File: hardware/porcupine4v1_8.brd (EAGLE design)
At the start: 24.4 x 27.4 mm, 33 parts, among them X1 PROGCON

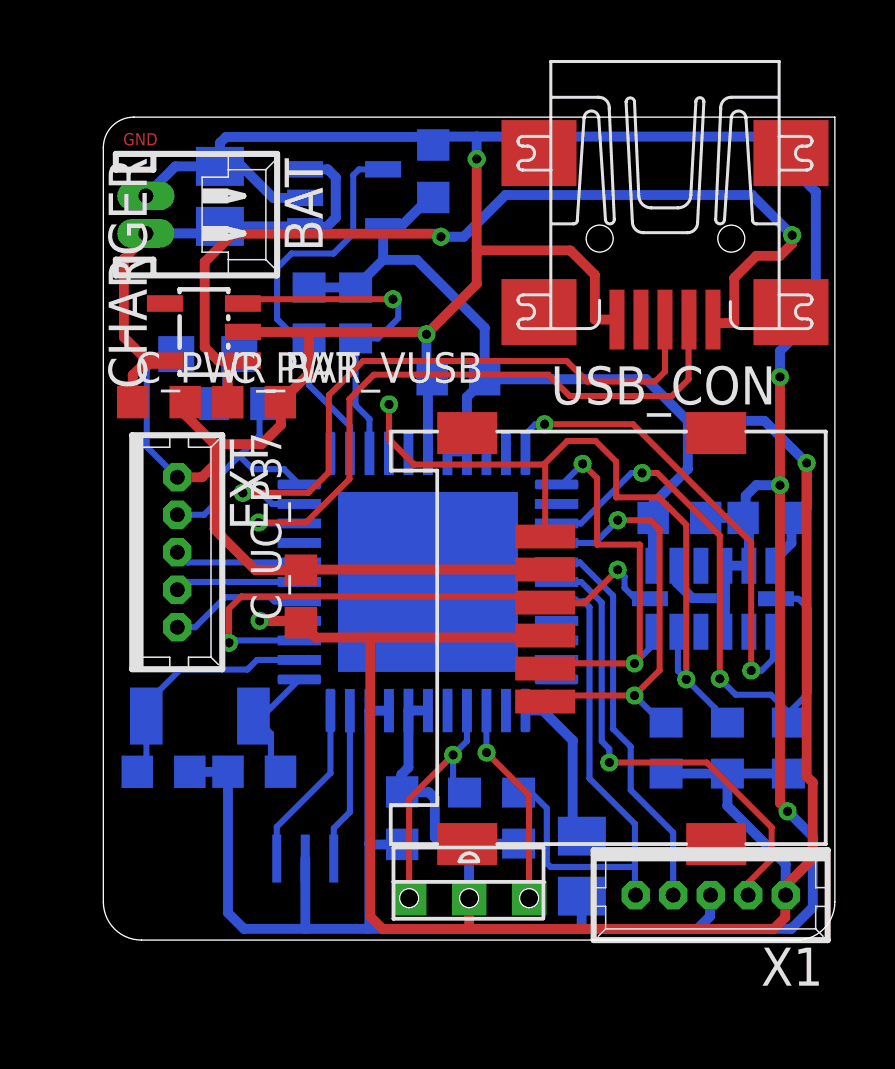
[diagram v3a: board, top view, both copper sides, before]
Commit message: porcupine4v1_8: updated extension pins (names), shifted some vias
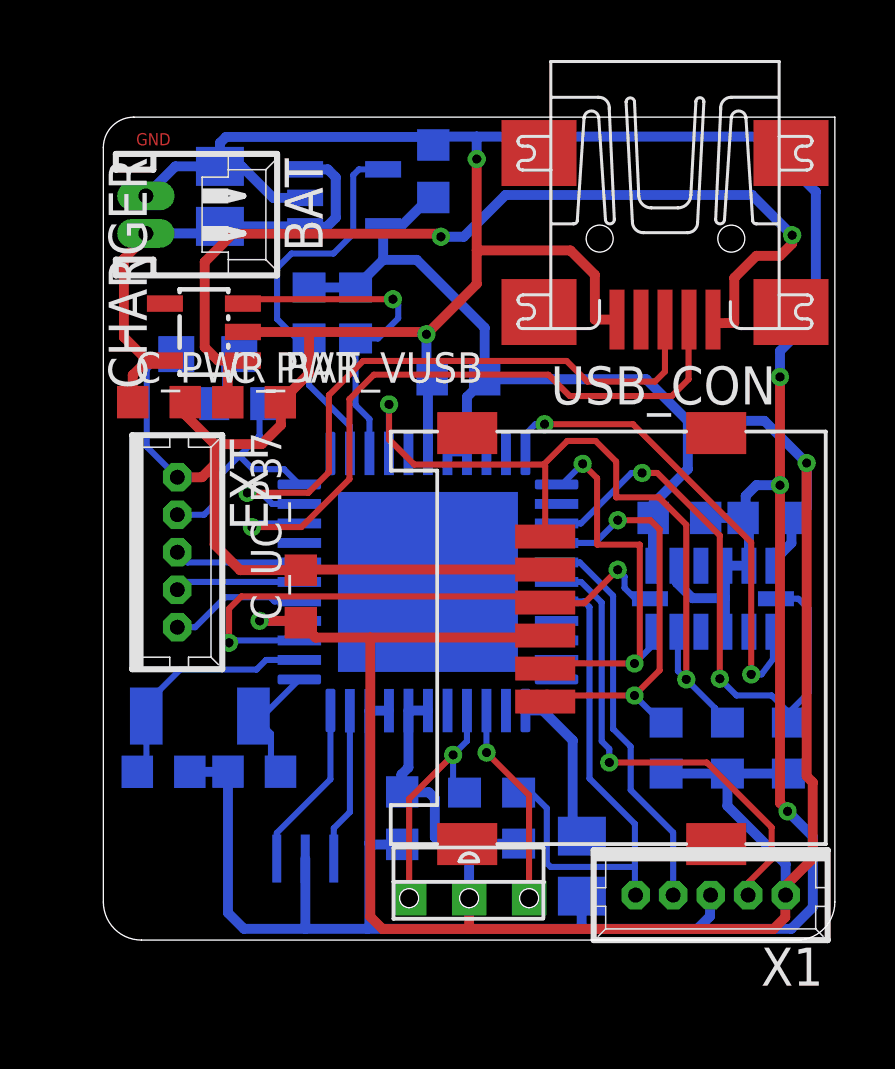
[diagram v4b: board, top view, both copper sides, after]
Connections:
- removed net EXT5: EXT.4, PIC_CONTROLLER.44, R8.2
- net EXT4: now also EXT.4, PIC_CONTROLLER.44, R8.2; no longer PIC_CONTROLLER.41
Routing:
- net EXT5: track 7.95 -> 0.00 mm
- net EXT4: track 0.00 -> 7.95 mm
- net USB_D-@RC4: track 21.8 -> 22.4 mm
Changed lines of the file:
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@@
 <wire x1="24.384" y1="1.27" x2="23.114" y2="0" width="0.0254" layer="20" curve="-90.027075"/>
 <wire x1="23.114" y1="0" x2="1.27" y2="0" width="0.0254" layer="20"/>
-<text x="0.6604" y="26.4922" size="0.4064" layer="1" font="vector" ratio="15">GND</text>
+<text x="1.0922" y="26.4922" size="0.4064" layer="1" font="vector" ratio="15">GND</text>
 </plain>
 <attributes>
@@
 <wire x1="12.446" y1="22.987" x2="12.446" y2="26.035" width="0.3302" layer="1"/>
 <wire x1="16.383" y1="20.6844" x2="17.1216" y2="20.6844" width="0.3302" layer="1"/>
-<wire x1="5.0686" y1="12.3304" x2="3.7084" y2="13.6906" width="0.3302" layer="1"/>
+<wire x1="4.5606" y1="12.3304" x2="3.7084" y2="13.1826" width="0.3302" layer="1"/>
 <wire x1="4.6876" y1="0.3756" x2="4.1542" y2="0.909" width="0.3302" layer="16"/>
 <wire x1="4.1542" y1="0.909" x2="4.1542" y2="5.6134" width="0.3302" layer="16"/>
@@
 <wire x1="14.7292" y1="12.3504" x2="6.5614" y2="12.3504" width="0.3302" layer="1"/>
 <wire x1="6.5614" y1="12.3504" x2="6.5814" y2="12.3304" width="0.3302" layer="1"/>
-<wire x1="5.0686" y1="12.3304" x2="6.5814" y2="12.3304" width="0.3302" layer="1"/>
+<wire x1="4.5606" y1="12.3304" x2="6.5814" y2="12.3304" width="0.3302" layer="1"/>
 <wire x1="23.749" y1="24.9428" x2="21.9088" y2="26.783" width="0.3302" layer="16"/>
 <wire x1="21.9088" y1="26.783" x2="12.446" y2="26.783" width="0.3302" layer="16"/>
@@
 <wire x1="5.8982" y1="17.927" x2="6.858" y2="18.8868" width="0.3302" layer="1"/>
 <wire x1="6.858" y1="18.8868" x2="6.858" y2="20.2692" width="0.3302" layer="1"/>
-<wire x1="3.7084" y1="13.6906" x2="3.7084" y2="15.8496" width="0.3302" layer="1"/>
+<wire x1="3.7084" y1="13.1826" x2="3.7084" y2="15.8496" width="0.3302" layer="1"/>
 <wire x1="3.7084" y1="15.8496" x2="3.7084" y2="16.5322" width="0.3302" layer="1"/>
 <wire x1="2.7292" y1="17.9324" x2="2.7292" y2="17.5114" width="0.3302" layer="1"/>
@@
 <wire x1="7.5184" y1="15.5956" x2="7.5184" y2="18.161" width="0.2032" layer="1"/>
 <wire x1="7.5184" y1="18.161" x2="8.6614" y2="19.304" width="0.2032" layer="1"/>
-<via x="4.6482" y="14.9098" extent="1-16" drill="0.3048" shape="octagon"/>
+<via x="4.8006" y="14.9098" extent="1-16" drill="0.3048" shape="octagon"/>
 <wire x1="6.5329" y1="14.538" x2="5.6296" y2="14.538" width="0.2032" layer="16"/>
 <wire x1="5.6296" y1="14.538" x2="5.2578" y2="14.9098" width="0.2032" layer="16"/>
-<wire x1="5.2578" y1="14.9098" x2="4.6482" y2="14.9098" width="0.2032" layer="16"/>
+<wire x1="5.2578" y1="14.9098" x2="4.8006" y2="14.9098" width="0.2032" layer="16"/>
 <wire x1="7.5184" y1="15.5956" x2="6.8326" y2="14.9098" width="0.2032" layer="1"/>
-<wire x1="6.8326" y1="14.9098" x2="4.6482" y2="14.9098" width="0.2032" layer="1"/>
+<wire x1="6.8326" y1="14.9098" x2="4.8006" y2="14.9098" width="0.2032" layer="1"/>
 </signal>
 <signal name="USB_D-@RC4">
@@
 <wire x1="19.5072" y1="20.543" x2="19.5216" y2="20.6844" width="0.2032" layer="1"/>
 <wire x1="19.5072" y1="18.6944" x2="19.5072" y2="20.543" width="0.2032" layer="1"/>
-<wire x1="5.2256" y1="13.887" x2="5.1816" y2="13.9192" width="0.2032" layer="16"/>
-<wire x1="6.5339" y1="13.887" x2="5.2256" y2="13.887" width="0.2032" layer="16"/>
+<wire x1="5.0732" y1="13.887" x2="4.953" y2="13.7668" width="0.2032" layer="16"/>
+<wire x1="6.5339" y1="13.887" x2="5.0732" y2="13.887" width="0.2032" layer="16"/>
 <wire x1="18.9484" y1="18.1356" x2="19.5072" y2="18.6944" width="0.2032" layer="1"/>
 <wire x1="9.017" y1="18.8468" x2="14.8336" y2="18.8468" width="0.2032" layer="1"/>
@@
 <wire x1="8.2042" y1="15.367" x2="8.2042" y2="18.034" width="0.2032" layer="1"/>
 <wire x1="8.2042" y1="18.034" x2="9.017" y2="18.8468" width="0.2032" layer="1"/>
-<via x="5.1816" y="13.9192" extent="1-16" drill="0.3048" shape="octagon"/>
+<via x="4.953" y="13.7668" extent="1-16" drill="0.3048" shape="octagon"/>
 <wire x1="14.8336" y1="18.8468" x2="15.5448" y2="18.1356" width="0.2032" layer="1"/>
-<wire x1="8.2042" y1="15.367" x2="6.7564" y2="13.9192" width="0.2032" layer="1"/>
-<wire x1="6.7564" y1="13.9192" x2="5.1816" y2="13.9192" width="0.2032" layer="1"/>
+<wire x1="8.2042" y1="15.367" x2="6.604" y2="13.7668" width="0.2032" layer="1"/>
+<wire x1="6.604" y1="13.7668" x2="4.953" y2="13.7668" width="0.2032" layer="1"/>
 </signal>
 <signal name="V_USB">
@@
 <wire x1="20.5486" y1="13.4874" x2="20.5486" y2="8.7122" width="0.2032" layer="1"/>
 <via x="20.5486" y="8.7122" extent="1-16" drill="0.3048" shape="octagon"/>
-<wire x1="20.5486" y1="8.7122" x2="21.082" y2="8.1788" width="0.2032" layer="16"/>
-<wire x1="21.082" y1="8.1788" x2="22.2504" y2="8.1788" width="0.2032" layer="16"/>
+<wire x1="20.5486" y1="8.7122" x2="21.1074" y2="8.1534" width="0.2032" layer="16"/>
+<wire x1="21.1074" y1="8.1534" x2="22.2758" y2="8.1534" width="0.2032" layer="16"/>
 <wire x1="22.8346" y1="7.2508" x2="22.8346" y2="7.5692" width="0.2032" layer="16"/>
-<wire x1="22.8346" y1="7.5946" x2="22.2504" y2="8.1788" width="0.2032" layer="16"/>
+<wire x1="22.8346" y1="7.5946" x2="22.2758" y2="8.1534" width="0.2032" layer="16"/>
 <wire x1="23.5204" y1="8.255" x2="22.8346" y2="7.5692" width="0.2032" layer="16"/>
 <wire x1="22.8346" y1="7.5692" x2="22.8346" y2="7.5946" width="0.2032" layer="16"/>
@@
 <contactref element="PIC_CONTROLLER" pad="35"/>
 <contactref element="32KHZ_CRYSTAL" pad="P$1"/>
-<wire x1="6.5329" y1="9.338" x2="5.1216" y2="9.338" width="0.2032" layer="16"/>
-<wire x1="5.1216" y1="9.338" x2="4.8006" y2="9.017" width="0.2032" layer="16"/>
-<wire x1="4.8006" y1="9.017" x2="2.5654" y2="9.017" width="0.2032" layer="16"/>
+<wire x1="6.5329" y1="9.338" x2="5.4264" y2="9.338" width="0.2032" layer="16"/>
+<wire x1="5.4264" y1="9.338" x2="5.1054" y2="9.017" width="0.2032" layer="16"/>
+<wire x1="5.1054" y1="9.017" x2="2.5654" y2="9.017" width="0.2032" layer="16"/>
 <wire x1="2.5654" y1="9.017" x2="1.4478" y2="7.8994" width="0.2032" layer="16"/>
 <wire x1="1.4478" y1="7.8994" x2="1.4318" y2="7.4676" width="0.2032" layer="16"/>
@@
 <contactref element="PIC_CONTROLLER" pad="11"/>
 <wire x1="22.32" y1="9.3638" x2="22.32" y2="10.2792" width="0.2032" layer="16"/>
-<wire x1="21.9402" y1="8.984" x2="22.32" y2="9.3638" width="0.2032" layer="16"/>
-<wire x1="21.596" y1="8.984" x2="21.9402" y2="8.984" width="0.2032" layer="16"/>
+<wire x1="21.9402" y1="8.857" x2="22.32" y2="9.3638" width="0.2032" layer="16"/>
+<wire x1="21.596" y1="8.857" x2="21.9402" y2="8.857" width="0.2032" layer="16"/>
 <wire x1="14.7066" y1="17.1958" x2="17.653" y2="17.1958" width="0.2032" layer="1"/>
 <wire x1="14.4018" y1="17.1958" x2="14.7066" y2="17.1958" width="0.2032" layer="16"/>
 <wire x1="14.0716" y1="16.8597" x2="14.4018" y2="17.1958" width="0.2032" layer="16"/>
 <wire x1="14.0704" y1="16.2235" x2="14.0716" y2="16.8597" width="0.2032" layer="16"/>
-<via x="21.596" y="8.984" extent="1-16" drill="0.3048" shape="octagon"/>
+<via x="21.596" y="8.857" extent="1-16" drill="0.3048" shape="octagon"/>
 <via x="14.7066" y="17.1958" extent="1-16" drill="0.3048" shape="octagon"/>
 <wire x1="17.653" y1="17.1958" x2="21.596" y2="13.2528" width="0.2032" layer="1"/>
-<wire x1="21.596" y1="13.2528" x2="21.596" y2="8.984" width="0.2032" layer="1"/>
+<wire x1="21.596" y1="13.2528" x2="21.596" y2="8.857" width="0.2032" layer="1"/>
 </signal>
 <signal name="V_BAT">
@@
 <contactref element="PIC_CONTROLLER" pad="33"/>
 <contactref element="12MHZ_RESONATOR" pad="1"/>
-<wire x1="5.781" y1="2.7178" x2="5.781" y2="3.7744" width="0.2032" layer="16"/>
-<wire x1="5.781" y1="3.7744" x2="7.5704" y2="5.5638" width="0.2032" layer="16"/>
-<wire x1="7.5704" y1="5.5638" x2="7.5704" y2="7.6535" width="0.2032" layer="16"/>
+<wire x1="5.781" y1="2.7178" x2="5.781" y2="3.5712" width="0.2032" layer="16"/>
+<wire x1="5.781" y1="3.5712" x2="7.5704" y2="5.3606" width="0.2032" layer="16"/>
+<wire x1="7.5704" y1="5.3606" x2="7.5704" y2="7.6535" width="0.2032" layer="16"/>
 </signal>
 <signal name="L_GND@RE0">
@@
 <wire x1="2.8054" y1="12.587" x2="2.4638" y2="12.9286" width="0.2032" layer="16"/>
 </signal>
+<signal name="N$4">
+<contactref element="LED1" pad="A"/>
+<contactref element="R8" pad="1"/>
+<wire x1="3.6966" y1="17.8816" x2="4.064" y2="17.9578" width="0.2032" layer="16"/>
+<wire x1="4.064" y1="17.9578" x2="4.064" y2="19.5326" width="0.2032" layer="16"/>
+<wire x1="4.064" y1="19.5326" x2="4.5298" y2="19.5326" width="0.2032" layer="16"/>
+<wire x1="4.6872" y1="19.5326" x2="4.5298" y2="19.5326" width="0.2032" layer="16"/>
+</signal>
 <signal name="EXT4">
-<contactref element="PIC_CONTROLLER" pad="41"/>
-</signal>
-<signal name="EXT5">
 <contactref element="PIC_CONTROLLER" pad="44"/>
-<wire x1="6.5319" y1="15.188" x2="6.0227" y2="15.6972" width="0.2032" layer="16"/>
 <wire x1="6.0227" y1="15.6972" x2="4.9784" y2="15.6972" width="0.2032" layer="16"/>
 <contactref element="R8" pad="2"/>
@@
 <wire x1="3.7338" y1="14.5542" x2="3.7338" y2="15.3434" width="0.2032" layer="16"/>
 <wire x1="3.7338" y1="15.3434" x2="4.533" y2="16.1426" width="0.2032" layer="16"/>
-</signal>
-<signal name="N$4">
-<contactref element="LED1" pad="A"/>
-<contactref element="R8" pad="1"/>
-<wire x1="3.6966" y1="17.8816" x2="4.064" y2="17.9578" width="0.2032" layer="16"/>
-<wire x1="4.064" y1="17.9578" x2="4.064" y2="19.5326" width="0.2032" layer="16"/>
-<wire x1="4.064" y1="19.5326" x2="4.5298" y2="19.5326" width="0.2032" layer="16"/>
-<wire x1="4.6872" y1="19.5326" x2="4.5298" y2="19.5326" width="0.2032" layer="16"/>
+<wire x1="6.5319" y1="15.188" x2="6.0227" y2="15.6972" width="0.2032" layer="16"/>
 </signal>
 </signals>
